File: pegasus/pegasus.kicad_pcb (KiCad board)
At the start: 2 copper layers, 39 x 104.5 mm, 19 parts, among them IC1 L7805ACV, IC2 RFD900, IC3 L70B-M39, J1 Screw_Terminal_01x04, J2 Screw_Terminal_01x02, U1 Teensy4.0, U2 CON-SMA-EDGE-S, U3 CON-SMA-EDGE-S, U4 XTSD04GCLGEGA

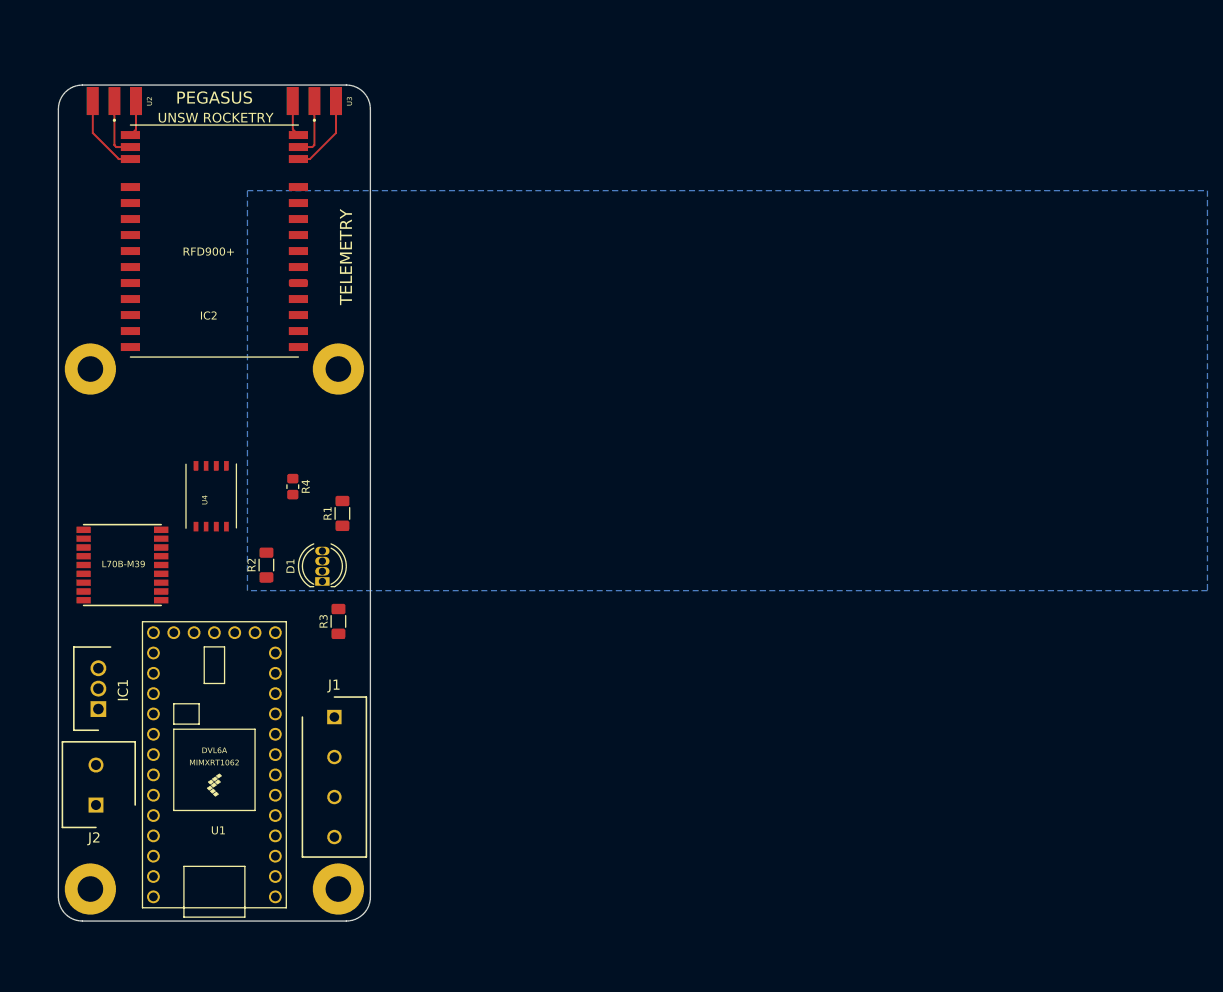
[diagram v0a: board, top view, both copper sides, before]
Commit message: add borders and titles to components in schematic
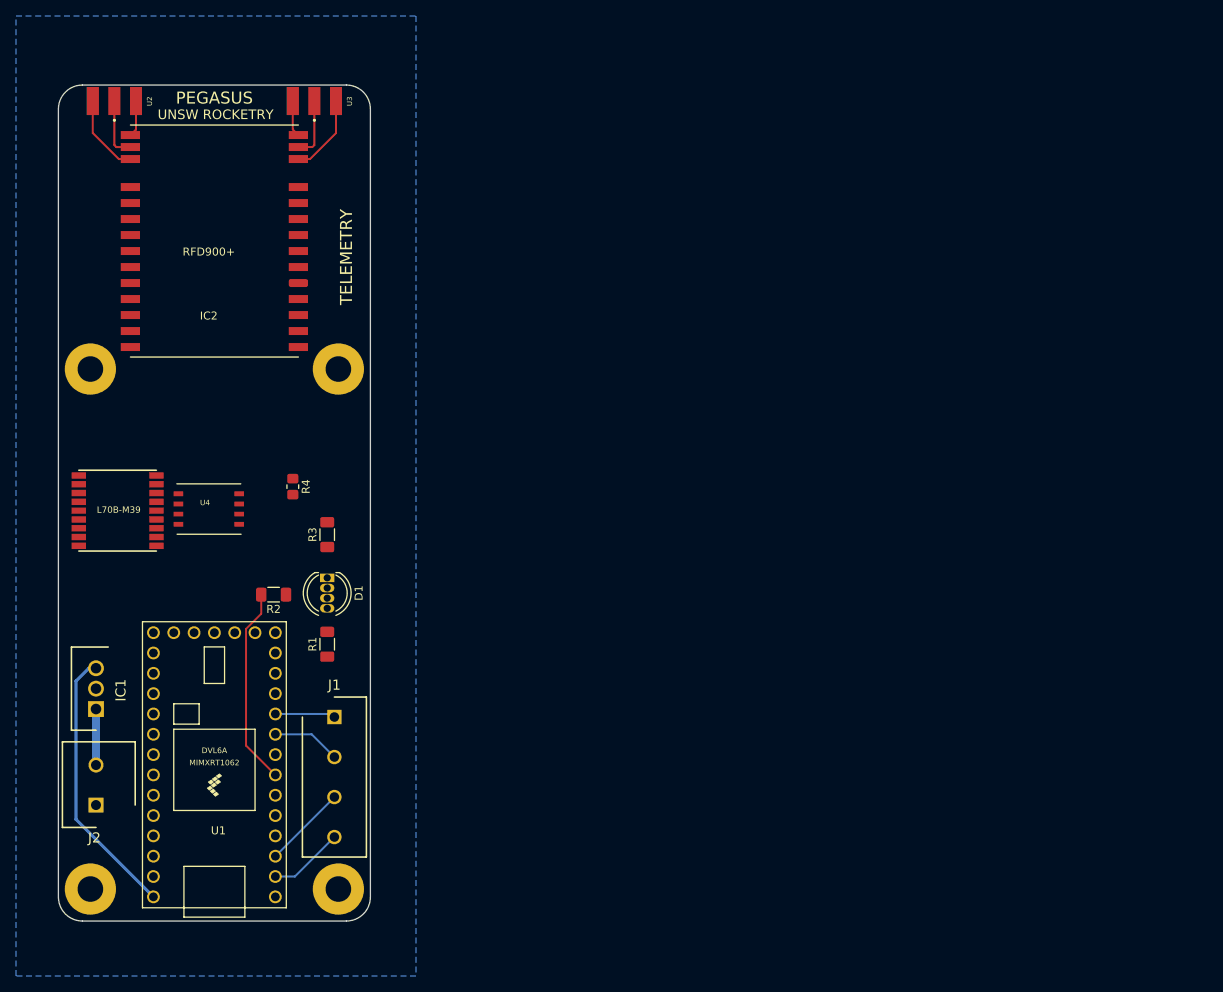
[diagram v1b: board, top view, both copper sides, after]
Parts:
- moved R1 16.5 mm to (119.6, 125.4)
- moved R3 10.9 mm to (119.6, 111.7)
- moved IC3 6.83 mm to (93.4, 108.7)
- moved R2 3.81 mm to (112.9, 119.2), turned to 180 degrees
- moved U4 1.63 mm to (104.8, 108.5), turned to 0 degrees
- moved D1 0.75 mm to (119.6, 117.1), turned to -90 degrees
- moved IC1 0.30 mm to (90.7, 133.5)
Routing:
- net +5V: track 0.00 -> 34.1 mm
- net RGB2: track 0.00 -> 24.8 mm
- net TX1: track 0.00 -> 10.5 mm
- net RX1: track 0.00 -> 9.42 mm
- net RX2: track 0.00 -> 8.56 mm
- net TX2: track 0.00 -> 7.54 mm
- net /BATT+: track 0.00 -> 7.00 mm

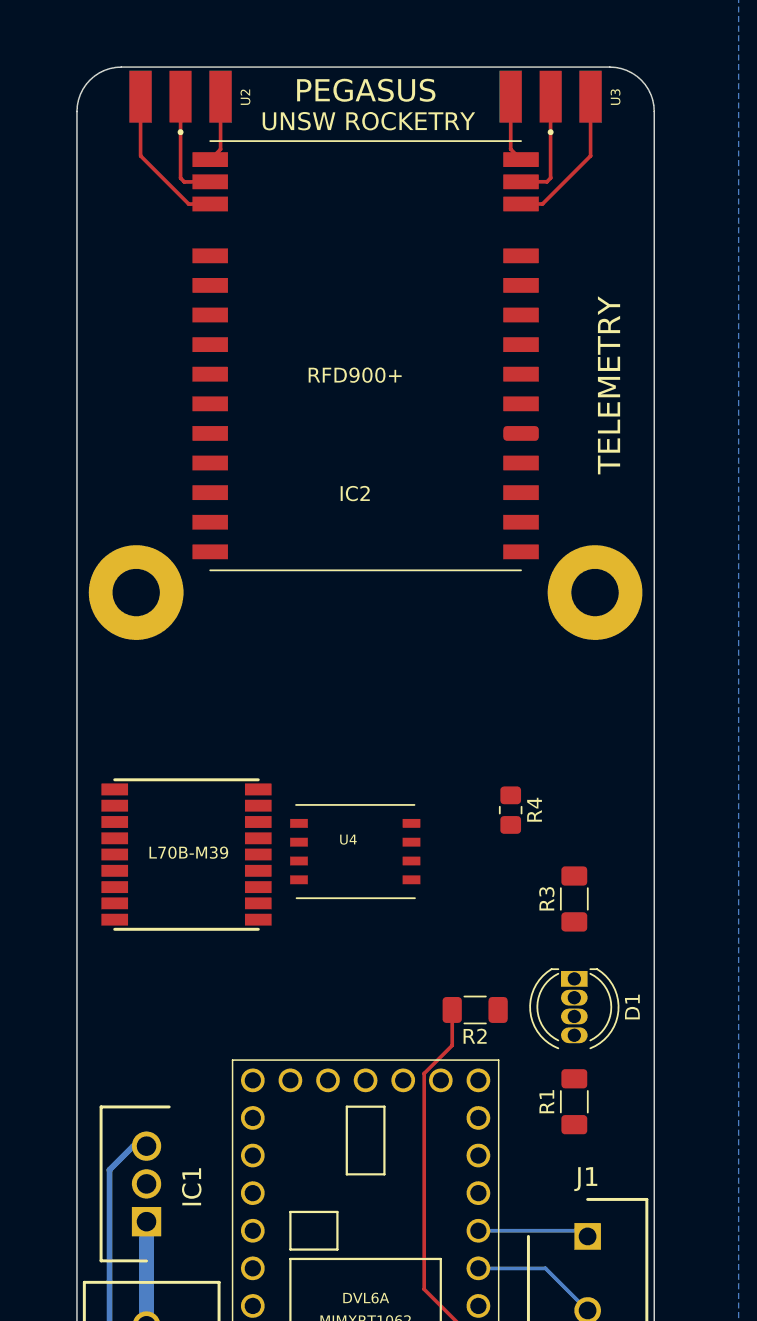
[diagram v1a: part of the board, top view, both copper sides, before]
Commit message: add some traces
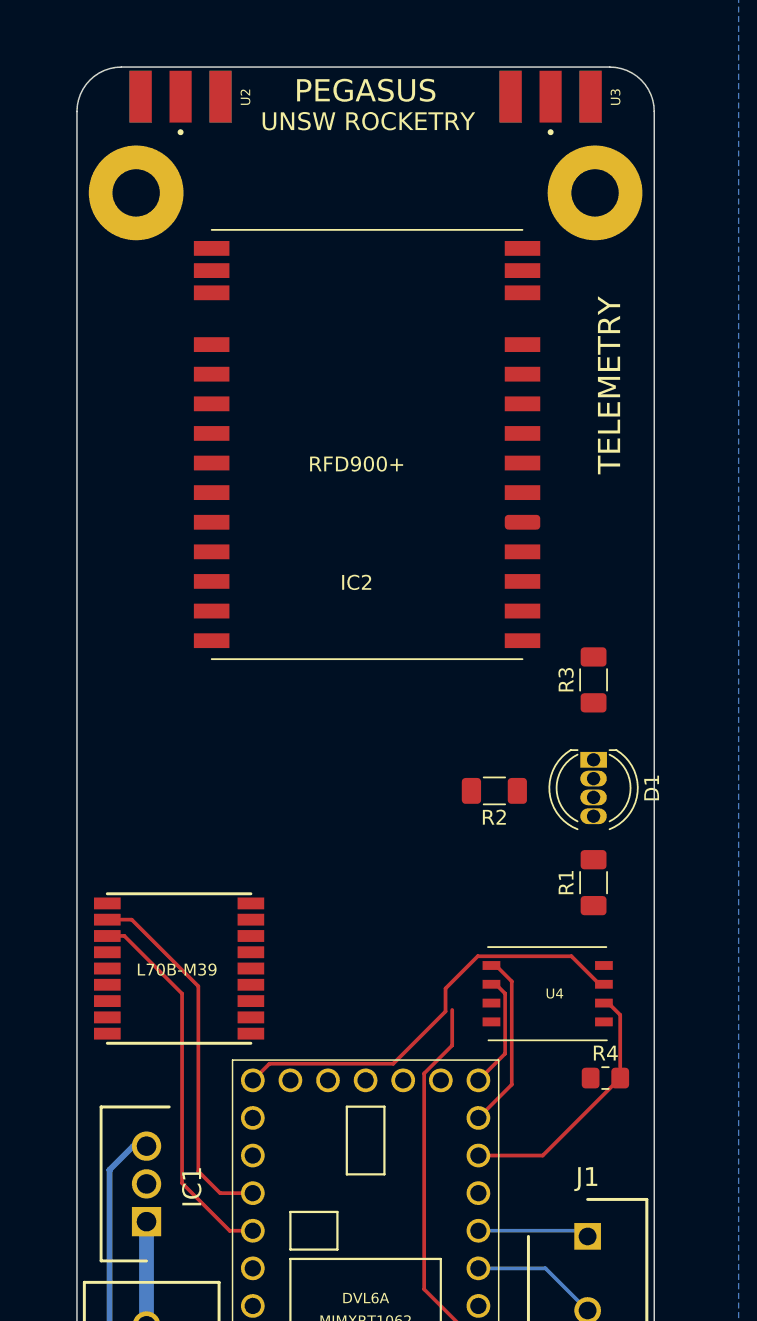
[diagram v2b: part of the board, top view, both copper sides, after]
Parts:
- moved H3 27.0 mm to (121.0, 64.0)
- moved H4 27.0 mm to (90.0, 64.0)
- moved R4 19.2 mm to (121.7, 123.8), turned to 0 degrees
- moved U4 16.2 mm to (117.8, 118.1), turned to 180 degrees
- moved R1 14.9 mm to (120.9, 110.6)
- moved D1 14.9 mm to (120.9, 102.3)
- moved R3 14.9 mm to (120.9, 96.9)
- moved R2 14.9 mm to (114.2, 104.4)
- moved IC3 7.72 mm to (92.9, 116.4), turned to 0 degrees
- moved IC2 6.00 mm to (110.1, 84.2)
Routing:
- net /SCK: track 0.00 -> 28.9 mm
- net TX4: track 0.00 -> 25.6 mm
- net RX4: track 0.00 -> 24.8 mm
- net /CS: track 0.00 -> 17.4 mm
- net /MOSI: track 0.00 -> 12.0 mm
- net Net-(IC2-Pad17): track 10.5 -> 0.00 mm
- net Net-(IC2-Pad12): track 10.5 -> 0.00 mm
- net Net-(IC2-Pad16): track 8.01 -> 0.00 mm
- net Net-(IC2-Pad13): track 8.01 -> 0.00 mm
- net /MISO: track 0.00 -> 7.80 mm
- net Net-(IC2-Pad15): track 4.95 -> 0.00 mm
- net Net-(IC2-Pad14): track 4.95 -> 0.00 mm

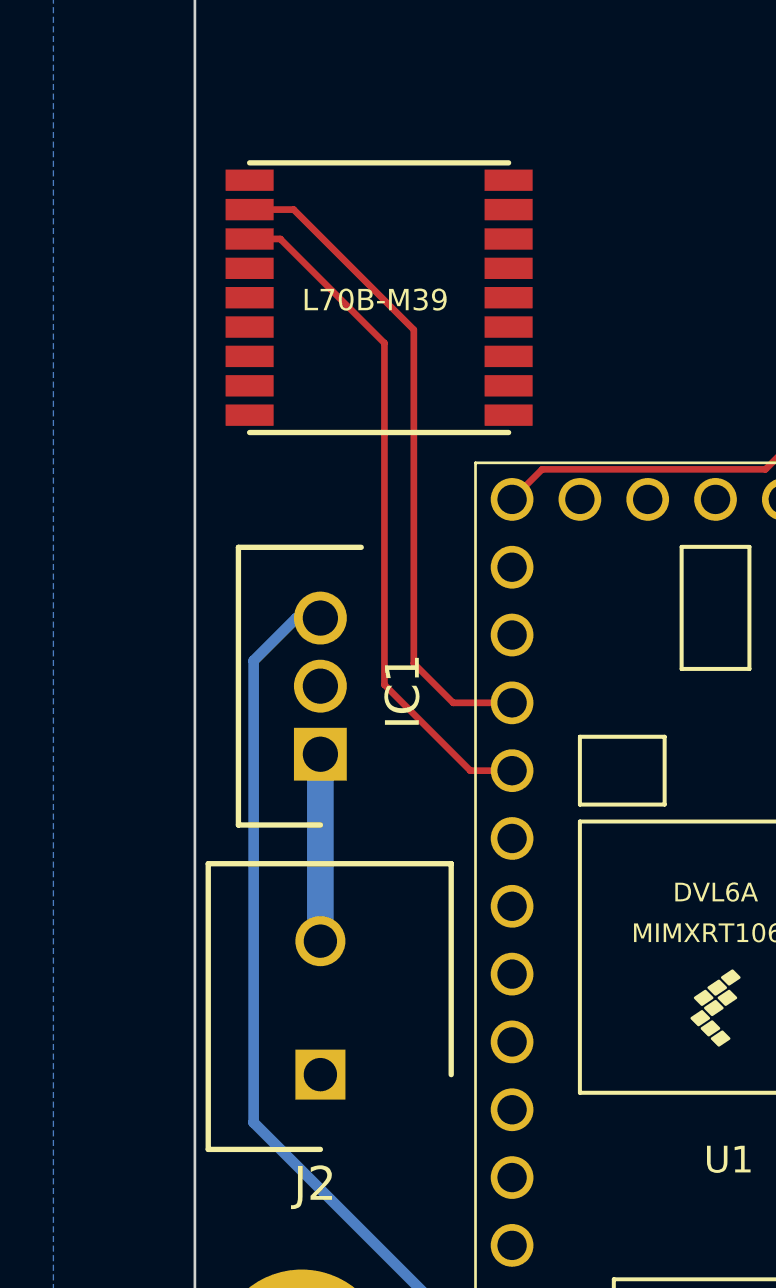
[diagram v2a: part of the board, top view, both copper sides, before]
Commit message: New voltage regulator added to schematic and pcb
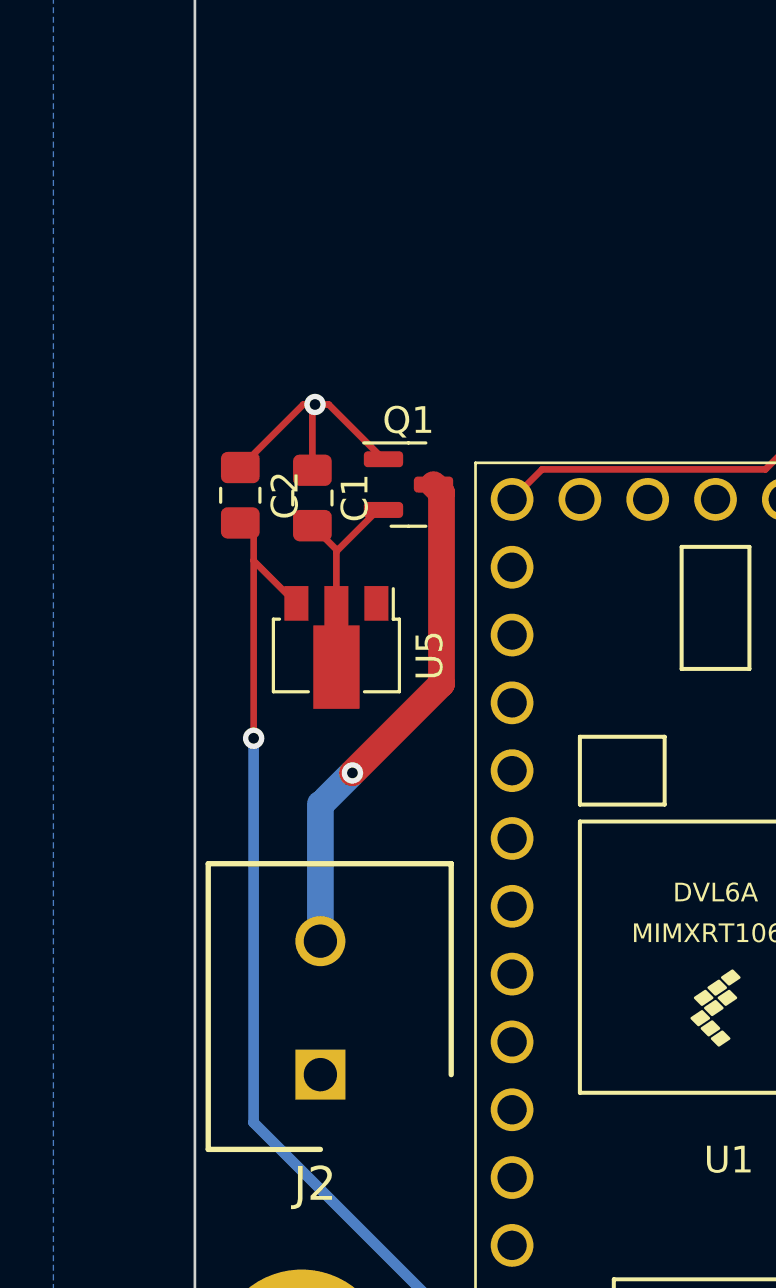
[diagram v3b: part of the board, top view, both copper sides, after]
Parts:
- removed IC1: L7805ACV, RS-Components:TO255P460X1020X2008-3P
- removed IC3: L70B-M39, Quectel_L70B-M39:1x18
- added C1: 1µF, Capacitor_SMD:C_0805_2012Metric_Pad1.18x1.45mm_HandSolder, F.Cu at (90.4, 123.9)
- added C2: 1µF, Capacitor_SMD:C_0805_2012Metric_Pad1.18x1.45mm_HandSolder, F.Cu at (87.7, 123.8)
- added Q1: ST3413A, Package_TO_SOT_SMD:SOT-23, F.Cu at (94.0, 123.4)
- added U5: HT7350-A, Package_TO_SOT_SMD:SOT-89-3, F.Cu at (91.3, 129.5)
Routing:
- net TX4: track 25.6 -> 0.00 mm
- net RX4: track 24.8 -> 0.00 mm
- net /BATT+: track 7.00 -> 18.9 mm, vias 0 -> 1
- net GND: track 0.00 -> 9.69 mm, vias 0 -> 1
- net Net-(C1-Pad2): track 0.00 -> 5.78 mm
- net +5V: track 34.1 -> 38.6 mm, vias 0 -> 1

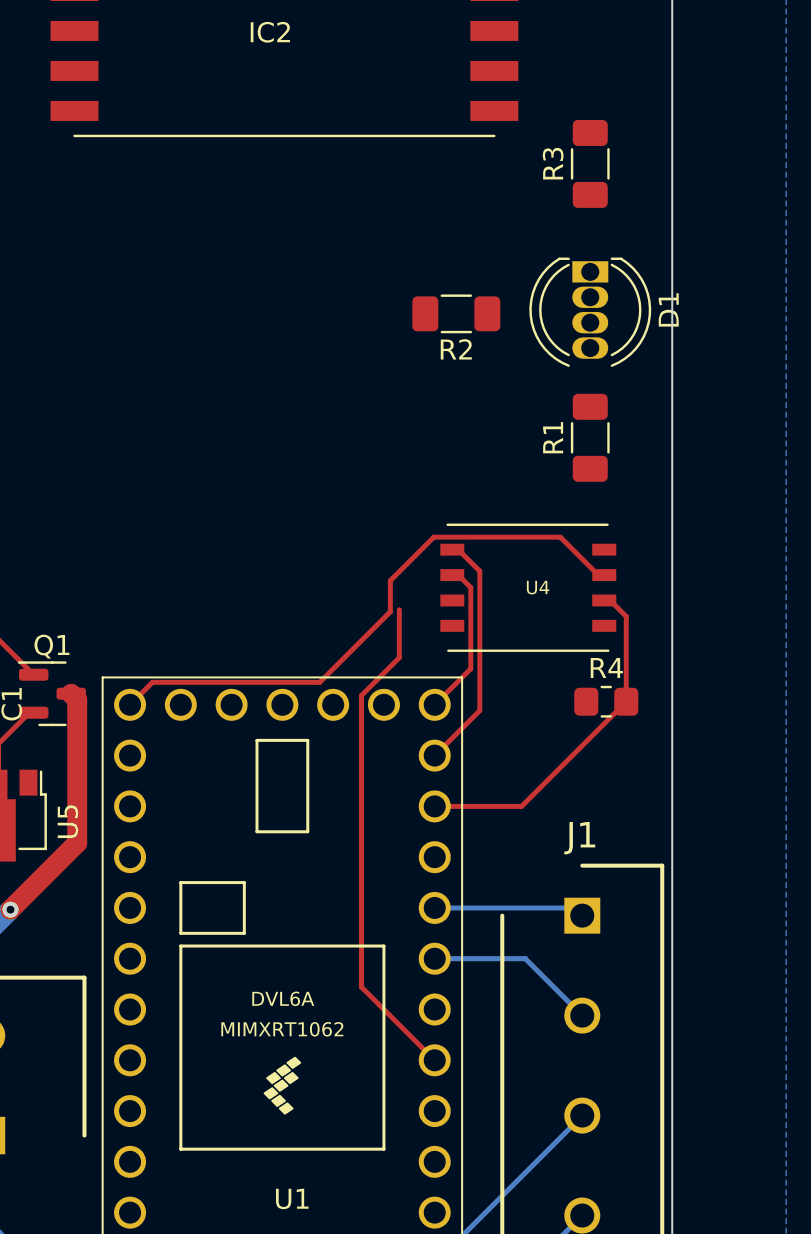
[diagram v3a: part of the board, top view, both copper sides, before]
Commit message: Route LED and memory on PCB
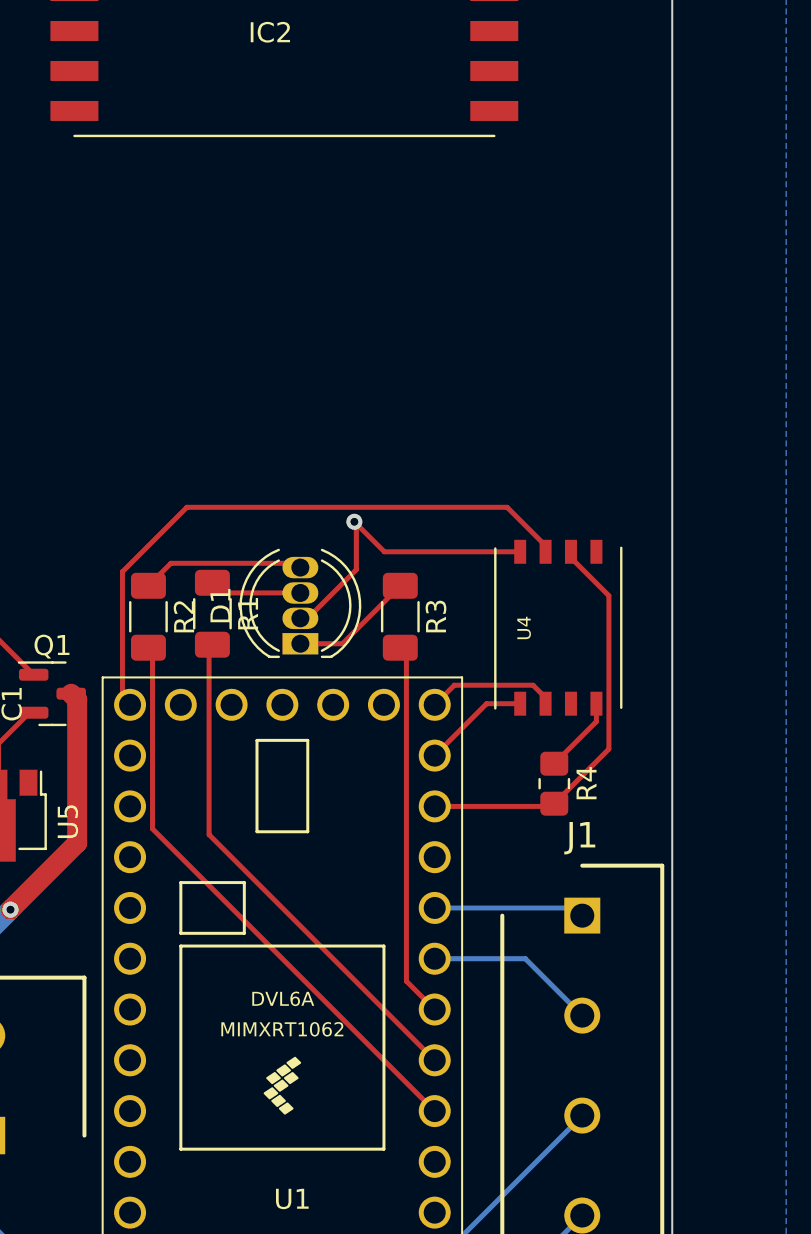
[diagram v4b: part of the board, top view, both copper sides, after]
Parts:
- moved R3 24.6 mm to (111.4, 119.5), turned to -90 degrees
- moved D1 23.6 mm to (106.4, 120.9), turned to 90 degrees
- moved R2 21.6 mm to (98.8, 119.5), turned to -90 degrees
- moved R1 20.8 mm to (102.0, 119.4), turned to -90 degrees
- moved R4 4.85 mm to (119.1, 127.9), turned to -90 degrees
- moved U4 2.50 mm to (119.3, 120.1), turned to -90 degrees
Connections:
- R1 pad 2: RGB1 -> RGB2
- R2 pad 2: RGB2 -> RGB1
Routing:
- net RGB1: track 0.00 -> 29.1 mm
- net RGB3: track 0.00 -> 18.8 mm
- net GND: track 9.69 -> 25.1 mm, vias 1 -> 2
- net Net-(D1-Pad4): track 0.00 -> 8.15 mm
- net /MOSI: track 12.0 -> 5.35 mm
- net Net-(D1-Pad1): track 0.00 -> 6.20 mm
- net Net-(D1-Pad3): track 0.00 -> 4.61 mm
- net +3.3V: track 0.00 -> 3.87 mm
- net /CS: track 17.4 -> 20.6 mm
- net /SCK: track 28.9 -> 30.4 mm
- net /MISO: track 7.80 -> 6.51 mm
- net RGB2: track 24.8 -> 25.5 mm
